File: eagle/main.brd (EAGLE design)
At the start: 98.7 x 90.2 mm, 13 parts, among them IC1 7805TV, U1 INA213AIDCKT, U2 LM1117MP-3.3

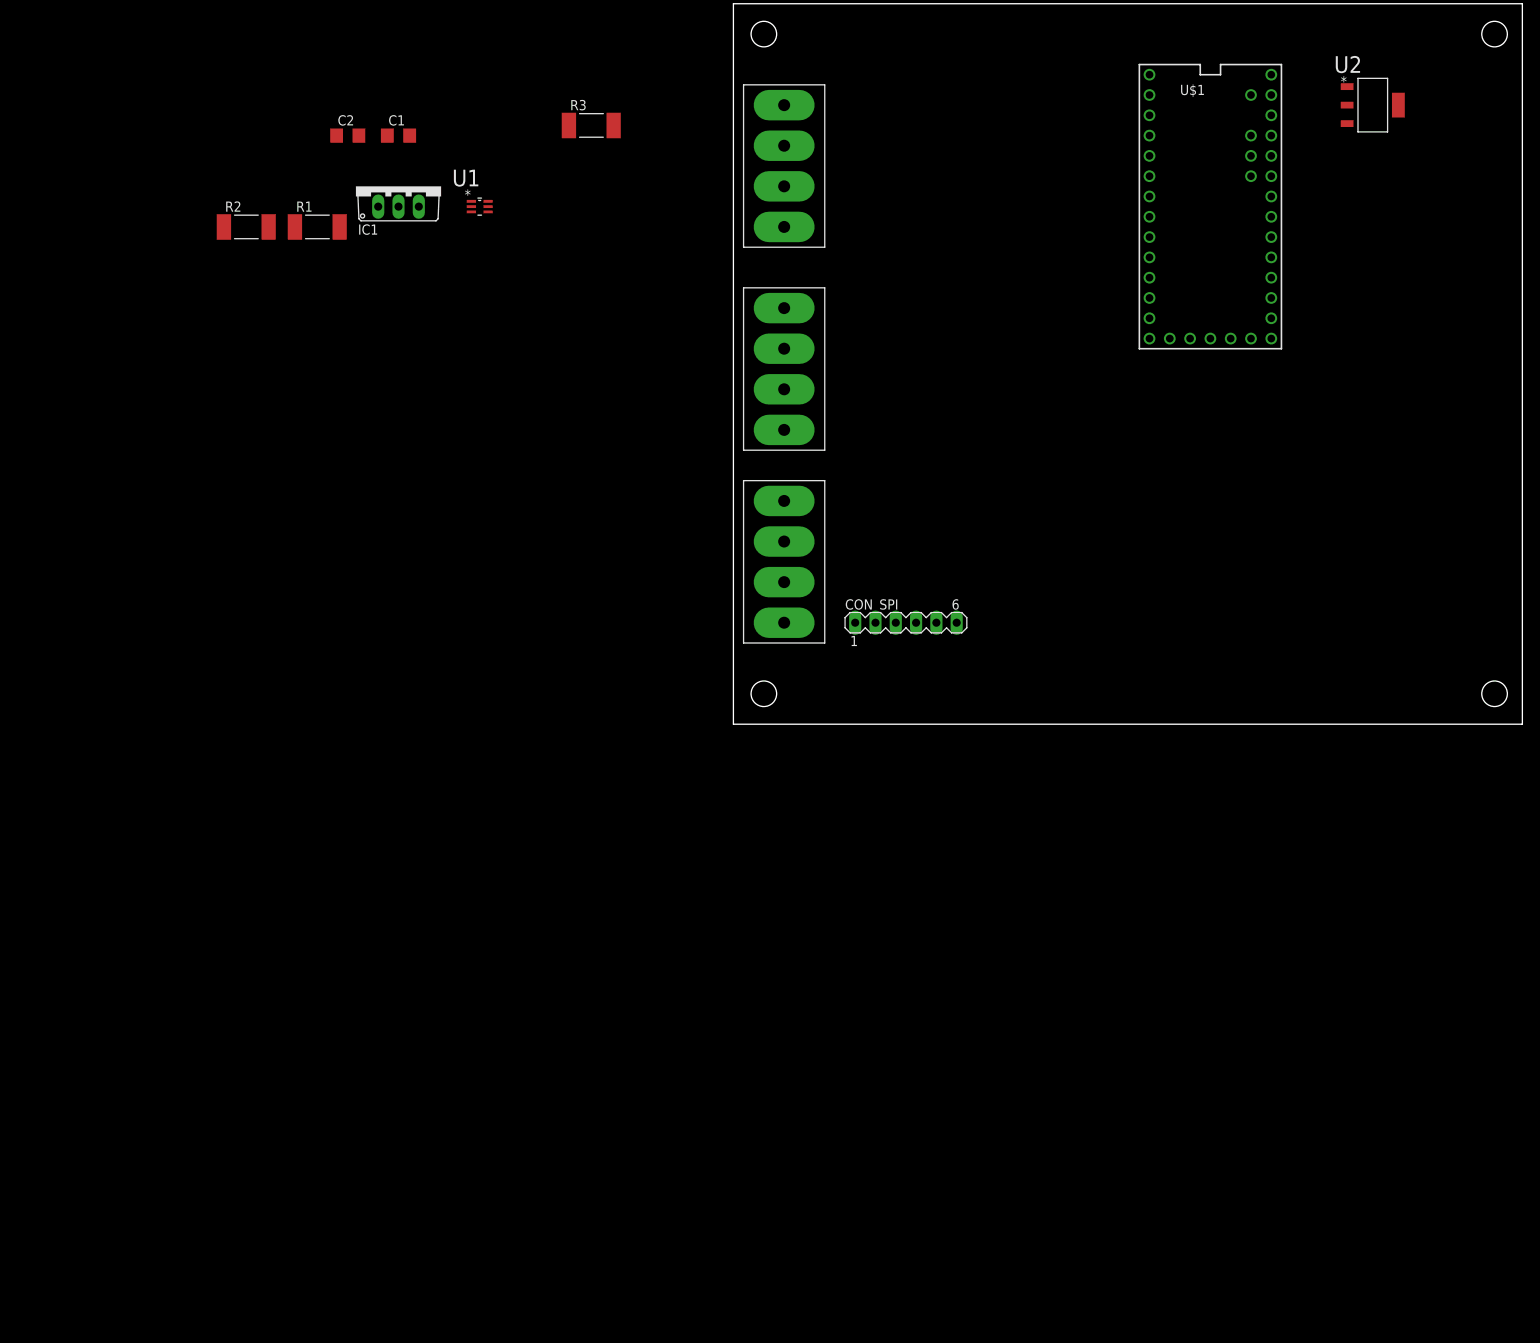
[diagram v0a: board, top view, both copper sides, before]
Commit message: add microsd
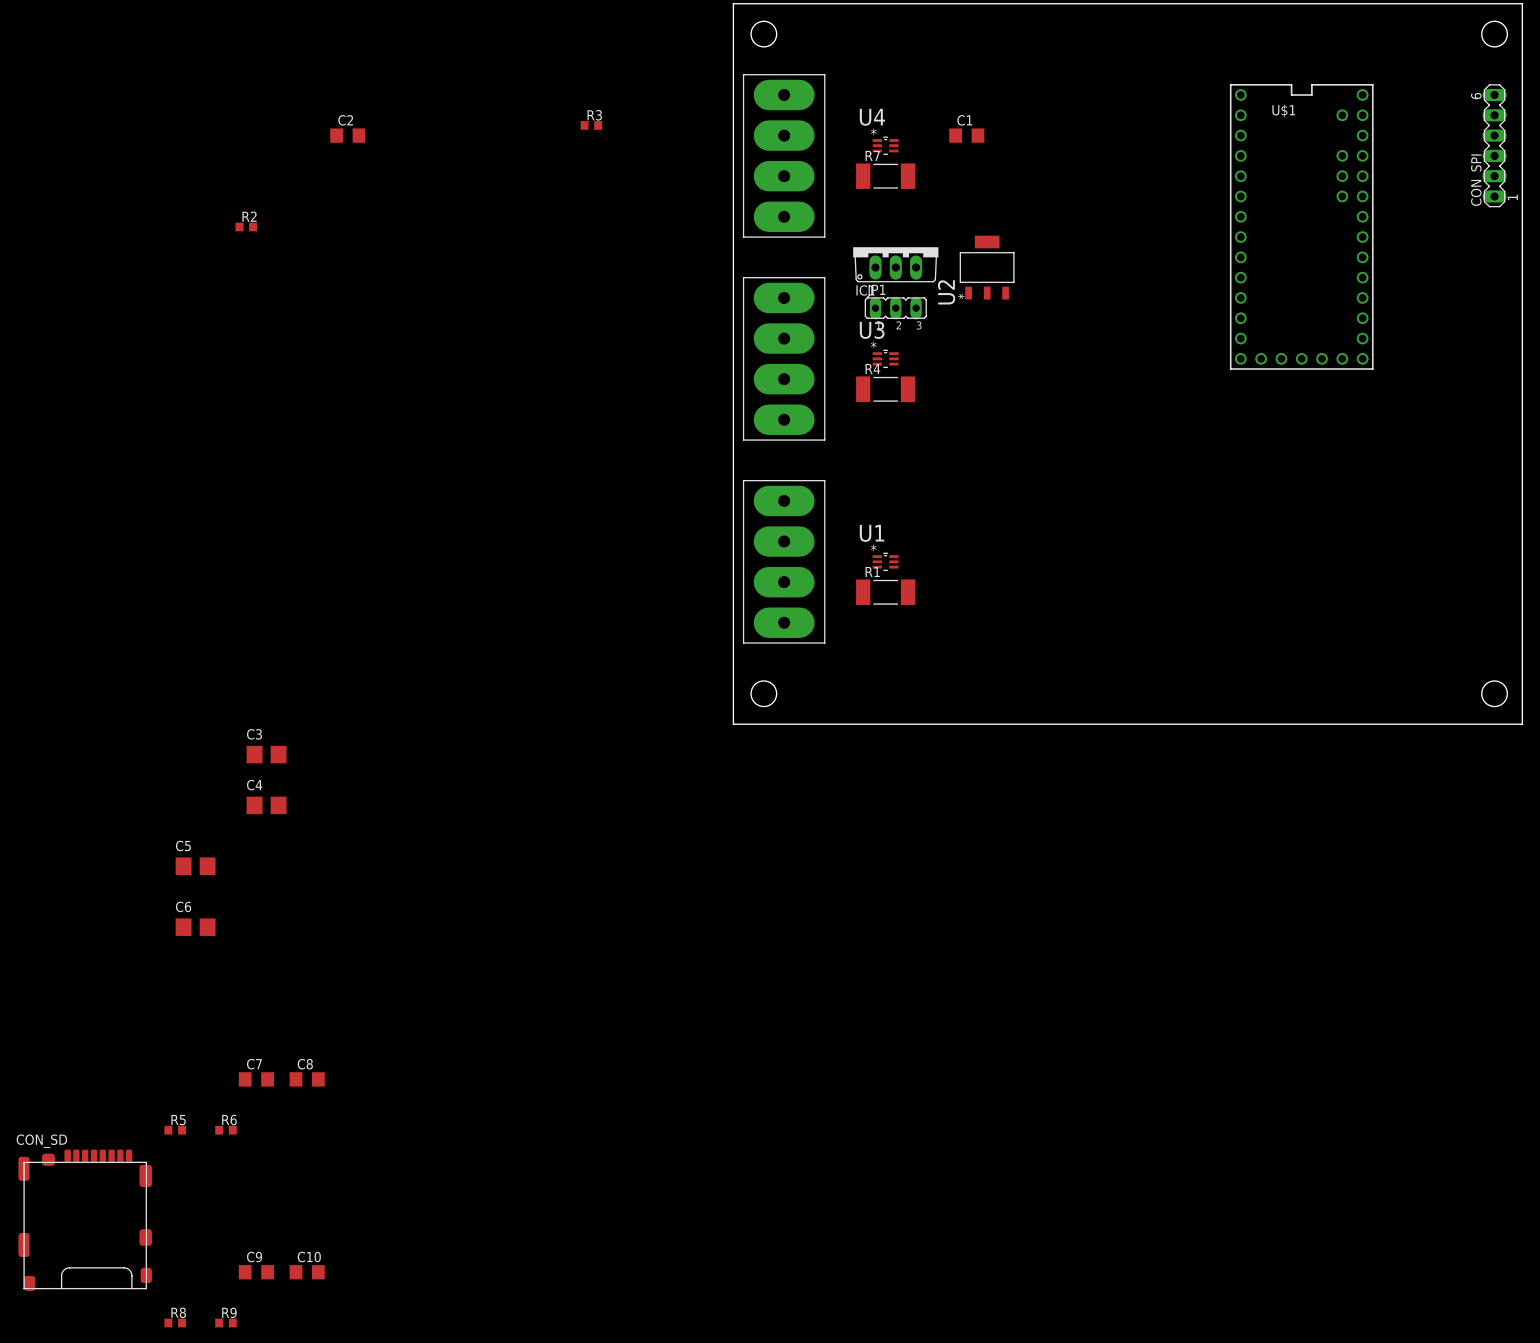
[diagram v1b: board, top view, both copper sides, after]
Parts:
- added C10, C7, C8, C9: 100n, rcl:C1206
- added C3, C4, C5, C6: 10u, rcl:CT3528
- added CON_SD: MICROSD_SPI_MODE, con-molex-microsd:MICRO_SD_CONNECTOR
- added JP1: (no value), jumper:JP2
- added R4, R7: 0.002, resistor:R2512
- added R5, R8: 470K, rcl:R0603
- added R6, R9: 20K, rcl:R0603
- added U3, U4: INA213AIDCKT, TI-INA213AIDCKT:SOT65P210X110-6N
- R2: value 96K -> 470K; device resistor:R2512 -> rcl:R0603
- R3: value 40K -> 20K; device resistor:R2512 -> rcl:R0603
- moved CON_SPI 94.8 mm to (95.2, 72.4), turned to 90 degrees
- moved R1 84.5 mm to (19.1, 16.5)
- moved C1 71.1 mm to (29.2, 73.7)
- moved U1 67.5 mm to (19.1, 20.3)
- moved IC1 62.7 mm to (20.3, 59.7)
- moved U2 52.4 mm to (31.8, 57.1), turned to 90 degrees
- moved U$1 11.7 mm to (71.1, 62.2)
- moved CON_BAT 1.27 mm to (6.35, 71.1)
- moved CON_LOAD 1.27 mm to (6.35, 45.7)
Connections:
- removed net VUSB: U$1.VUSB
- new net BAT_5V: C4.+, IC1.3, JP1.3
- new net BAT_ISENSE: U4.6
- new net BAT_VSENSE: C9.1, R8.1, R9.2
- new net DC_3V3: C6.+, U2.2, U2.4
- new net LOAD_ISENSE: U3.6
- new net LOAD_VSENSE: C7.1, R5.1, R6.2
- new net USB_5V: JP1.1, U$1.VUSB
- net BAT_IN: now also C3.+, IC1.1, R7.2, U4.4
- net BAT_OUT: now also R7.1, R8.2, U4.5
- net DC_5V: now also C10.1, C5.+, C8.1, JP1.2, U2.3, U3.3, U4.3
- net GND: now also C10.2, C3.-, C4.-, C5.-, C6.-, C7.2, C8.2, C9.2, IC1.2, R6.1, R9.1, U2.1, U3.1, U3.2, U4.1, U4.2
- net LOAD_IN: now also R4.2, U3.4
- net LOAD_OUT: now also R4.1, R5.2, U3.5
